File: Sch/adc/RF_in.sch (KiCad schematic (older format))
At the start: 72 parts, among them CN1 SMA, CN2 SMA, J3 JP2, J4 JP2, J5 JP2, J6 JP2, U1 LTC2292, U2 BGA2818, U3 TLV702, U4 BGA2818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

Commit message: Add parts
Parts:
- R13, R14, R15, R2, R3, R5, R6, R7, R8, R9: footprint (none) -> Resistors_SMD:R_0603
- R16: value 51 -> 50; footprint (none) -> Resistors_SMD:R_0603
- R17, R18, R19, R20: value 24.9 -> 25; footprint (none) -> Resistors_SMD:R_0603
- R4: value 50 -> 22; footprint (none) -> Resistors_SMD:R_0603
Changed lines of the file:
@@
 P 6850 1650
 F 0 "R17" V 6930 1650 50  0000 C CNN
-F 1 "24.9" V 6850 1650 50  0000 C CNN
-F 2 "" V 6780 1650 50  0001 C CNN
+F 1 "25" V 6850 1650 50  0000 C CNN
+F 2 "Resistors_SMD:R_0603" V 6780 1650 50  0001 C CNN
 F 3 "" H 6850 1650 50  0000 C CNN
 	1    6850 1650
@@
 P 6850 1950
 F 0 "R18" V 6930 1950 50  0000 C CNN
-F 1 "24.9" V 6850 1950 50  0000 C CNN
-F 2 "" V 6780 1950 50  0001 C CNN
+F 1 "25" V 6850 1950 50  0000 C CNN
+F 2 "Resistors_SMD:R_0603" V 6780 1950 50  0001 C CNN
 F 3 "" H 6850 1950 50  0000 C CNN
 	1    6850 1950
@@
 P 7000 1500
 F 0 "R19" V 7080 1500 50  0000 C CNN
-F 1 "24.9" V 7000 1500 50  0000 C CNN
-F 2 "" V 6930 1500 50  0001 C CNN
+F 1 "25" V 7000 1500 50  0000 C CNN
+F 2 "Resistors_SMD:R_0603" V 6930 1500 50  0001 C CNN
 F 3 "" H 7000 1500 50  0000 C CNN
 	1    7000 1500
@@
 P 7000 2100
 F 0 "R20" V 7080 2100 50  0000 C CNN
-F 1 "24.9" V 7000 2100 50  0000 C CNN
-F 2 "" V 6930 2100 50  0001 C CNN
+F 1 "25" V 7000 2100 50  0000 C CNN
+F 2 "Resistors_SMD:R_0603" V 6930 2100 50  0001 C CNN
 F 3 "" H 7000 2100 50  0000 C CNN
 	1    7000 2100
@@
 P 6450 2200
 F 0 "R16" V 6530 2200 50  0000 C CNN
-F 1 "51" V 6450 2200 50  0000 C CNN
-F 2 "" V 6380 2200 50  0001 C CNN
+F 1 "50" V 6450 2200 50  0000 C CNN
+F 2 "Resistors_SMD:R_0603" V 6380 2200 50  0001 C CNN
 F 3 "" H 6450 2200 50  0000 C CNN
 	1    6450 2200
@@
 F 0 "R15" V 3880 1950 50  0000 C CNN
 F 1 "DNL" V 3800 1950 50  0000 C CNN
-F 2 "" V 3730 1950 50  0001 C CNN
+F 2 "Resistors_SMD:R_0603" V 3730 1950 50  0001 C CNN
 F 3 "" H 3800 1950 50  0000 C CNN
 	1    3800 1950
@@
 F 0 "R2" V 1530 6100 50  0000 C CNN
 F 1 "10k" V 1450 6100 50  0000 C CNN
-F 2 "" V 1380 6100 50  0001 C CNN
+F 2 "Resistors_SMD:R_0603" V 1380 6100 50  0001 C CNN
 F 3 "" H 1450 6100 50  0000 C CNN
 	1    1450 6100
@@
 P 2300 4750
 F 0 "R4" V 2380 4750 50  0000 C CNN
-F 1 "50" V 2300 4750 50  0000 C CNN
-F 2 "" V 2230 4750 50  0001 C CNN
+F 1 "22" V 2300 4750 50  0000 C CNN
+F 2 "Resistors_SMD:R_0603" V 2230 4750 50  0001 C CNN
 F 3 "" H 2300 4750 50  0000 C CNN
 	1    2300 4750
@@
 F 0 "R3" H 1230 4600 50  0000 C CNN
 F 1 "10k" V 1150 4600 50  0000 C CNN
-F 2 "" V 1080 4600 50  0001 C CNN
+F 2 "Resistors_SMD:R_0603" V 1080 4600 50  0001 C CNN
 F 3 "" H 1150 4600 50  0000 C CNN
 	1    1150 4600
@@
 F 0 "R8" V 7380 3500 50  0000 C CNN
 F 1 "25" V 7300 3500 50  0000 C CNN
-F 2 "" V 7230 3500 50  0001 C CNN
+F 2 "Resistors_SMD:R_0603" V 7230 3500 50  0001 C CNN
 F 3 "" H 7300 3500 50  0000 C CNN
 	1    7300 3500
@@
 F 0 "R7" V 7380 3200 50  0000 C CNN
 F 1 "25" V 7300 3200 50  0000 C CNN
-F 2 "" V 7230 3200 50  0001 C CNN
+F 2 "Resistors_SMD:R_0603" V 7230 3200 50  0001 C CNN
 F 3 "" H 7300 3200 50  0000 C CNN
 	1    7300 3200
@@
 F 0 "R5" V 6830 2900 50  0000 C CNN
 F 1 "1k" V 6750 2900 50  0000 C CNN
-F 2 "" V 6680 2900 50  0001 C CNN
+F 2 "Resistors_SMD:R_0603" V 6680 2900 50  0001 C CNN
 F 3 "" H 6750 2900 50  0000 C CNN
 	1    6750 2900
@@
 F 0 "R6" V 7080 2900 50  0000 C CNN
 F 1 "1k" V 7000 2900 50  0000 C CNN
-F 2 "" V 6930 2900 50  0001 C CNN
+F 2 "Resistors_SMD:R_0603" V 6930 2900 50  0001 C CNN
 F 3 "" H 7000 2900 50  0000 C CNN
 	1    7000 2900
@@
 F 0 "R9" V 2530 4250 50  0000 C CNN
 F 1 "10k" V 2450 4250 50  0000 C CNN
-F 2 "" V 2380 4250 50  0001 C CNN
+F 2 "Resistors_SMD:R_0603" V 2380 4250 50  0001 C CNN
 F 3 "" H 2450 4250 50  0000 C CNN
 	1    2450 4250
@@
 F 0 "R13" V 4530 4650 50  0000 C CNN
 F 1 "22" V 4450 4650 50  0000 C CNN
-F 2 "" V 4380 4650 50  0001 C CNN
+F 2 "Resistors_SMD:R_0603" V 4380 4650 50  0001 C CNN
 F 3 "" H 4450 4650 50  0000 C CNN
 	1    4450 4650
@@
 F 0 "R14" V 4530 4750 50  0000 C CNN
 F 1 "22" V 4450 4750 50  0000 C CNN
-F 2 "" V 4380 4750 50  0001 C CNN
+F 2 "Resistors_SMD:R_0603" V 4380 4750 50  0001 C CNN
 F 3 "" H 4450 4750 50  0000 C CNN
 	1    4450 4750

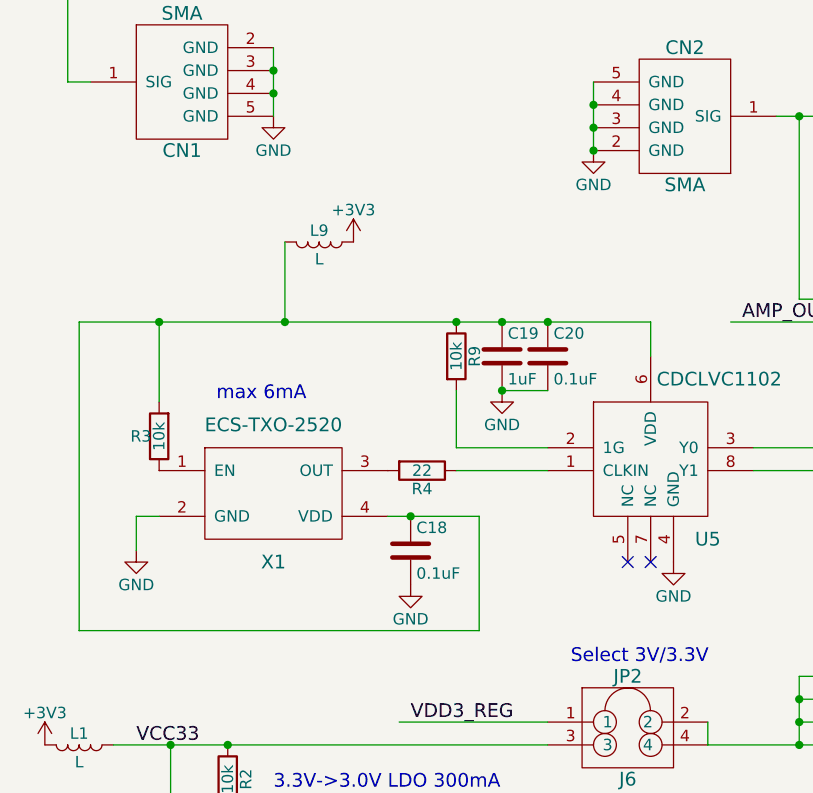
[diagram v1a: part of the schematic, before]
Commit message: Changed TCXO->MEMS TCXO. BOM finished
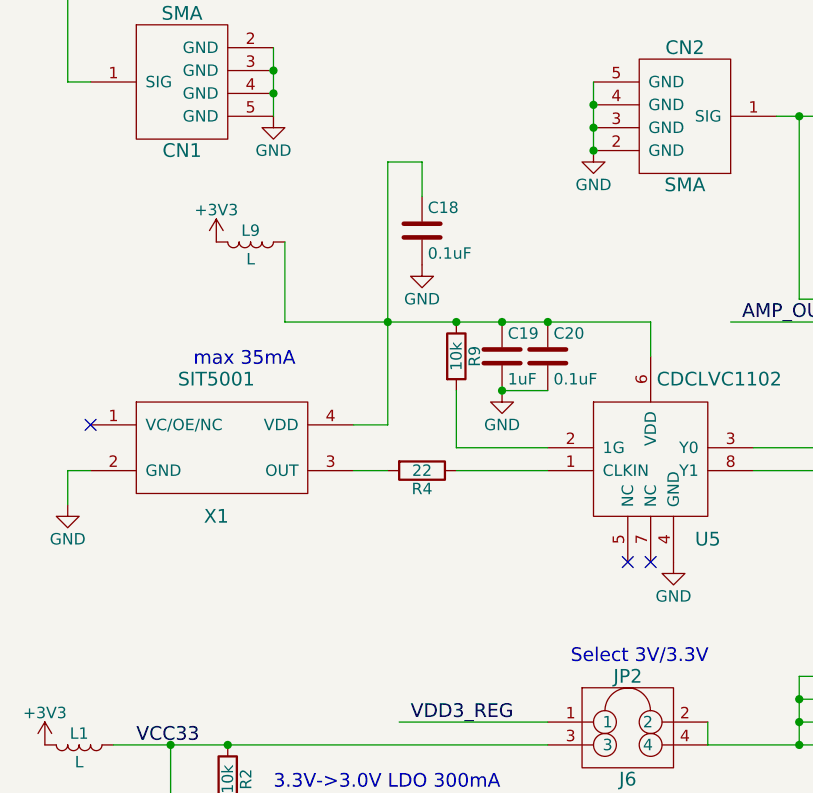
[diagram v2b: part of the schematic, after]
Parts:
- removed R3: 10k, Resistors_SMD:R_0603, symbol R
- removed X1: ECS-TXO-2520, symbol ECS-TXO-2520
- added X1: SIT5001, symbol SIT5001
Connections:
- no-connect marks 6 -> 7
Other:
- note added: "max 35mA"
- note removed: "max 6mA"
- moved on the sheet: C18, L9
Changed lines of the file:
@@
-$EndComp
-$Comp
-L ECS-TXO-2520 X1
-U 1 1 58A5DB2D
-P 1700 4850
-F 0 "X1" H 1650 4550 60  0000 C CNN
-F 1 "ECS-TXO-2520" H 1650 5150 60  0000 C CNN
-F 2 "" H 1700 4700 60  0001 C CNN
-F 3 "" H 1700 4700 60  0001 C CNN
-	1    1700 4850
-	1    0    0    -1
 $EndComp
 $Comp
@@
 L GND #PWR030
 U 1 1 58A651BF
-P 1050 5100
-F 0 "#PWR030" H 1050 4850 50  0001 C CNN
-F 1 "GND" H 1050 4950 50  0000 C CNN
-F 2 "" H 1050 5100 50  0000 C CNN
-F 3 "" H 1050 5100 50  0000 C CNN
-	1    1050 5100
+P 750 4900
+F 0 "#PWR030" H 750 4650 50  0001 C CNN
+F 1 "GND" H 750 4750 50  0000 C CNN
+F 2 "" H 750 4900 50  0000 C CNN
+F 3 "" H 750 4900 50  0000 C CNN
+	1    750  4900
 	1    0    0    -1
 $EndComp
@@
 	0    1    1    0
 $EndComp
-$Comp
-L R R3
-U 1 1 58A67F71
-P 1150 4600
-F 0 "R3" H 1230 4600 50  0000 C CNN
-F 1 "10k" V 1150 4600 50  0000 C CNN
-F 2 "Resistors_SMD:R_0603" V 1080 4600 50  0001 C CNN
-F 3 "" H 1150 4600 50  0000 C CNN
-	1    1150 4600
-	-1   0    0    1
-$EndComp
 Text Label 7250 2550 0    60   ~ 0
 CLK40M
@@
 Connection ~ 3950 5950
 Wire Wire Line
-	1150 4950 1050 4950
-Wire Wire Line
-	1050 4950 1050 5100
+	850  4750 750  4750
+Wire Wire Line
+	750  4750 750  4900
 Connection ~ 1200 5950
 Wire Wire Line
 	1450 6250 1450 6650
-Wire Wire Line
-	2150 4950 2550 4950
 Wire Wire Line
 	2450 4750 2850 4750
@@
 $EndComp
 Wire Wire Line
-	800  4100 3300 4100
+	1700 4100 3300 4100
 $Comp
 L +3V3 #PWR046
 U 1 1 58A88C4E
-P 2000 3750
-F 0 "#PWR046" H 2000 3600 50  0001 C CNN
-F 1 "+3V3" H 2000 3890 50  0000 C CNN
-F 2 "" H 2000 3750 50  0000 C CNN
-F 3 "" H 2000 3750 50  0000 C CNN
-	1    2000 3750
+P 1400 3750
+F 0 "#PWR046" H 1400 3600 50  0001 C CNN
+F 1 "+3V3" H 1400 3890 50  0000 C CNN
+F 2 "" H 1400 3750 50  0000 C CNN
+F 3 "" H 1400 3750 50  0000 C CNN
+	1    1400 3750
 	1    0    0    -1
 $EndComp
@@
 L L L9
 U 1 1 58A8A3F4
-P 1850 3750
-F 0 "L9" V 1800 3750 50  0000 C CNN
-F 1 "L" V 1925 3750 50  0000 C CNN
-F 2 "" H 1850 3750 50  0001 C CNN
-F 3 "" H 1850 3750 50  0000 C CNN
-	1    1850 3750
+P 1550 3750
+F 0 "L9" V 1500 3750 50  0000 C CNN
+F 1 "L" V 1625 3750 50  0000 C CNN
+F 2 "" H 1550 3750 50  0001 C CNN
+F 3 "" H 1550 3750 50  0000 C CNN
+	1    1550 3750
 	0    1    1    0
 $EndComp
-Wire Wire Line
-	1150 4450 1150 4100
-Wire Wire Line
-	2550 4950 2550 5450
-Wire Wire Line
-	2550 5450 800  5450
-Wire Wire Line
-	800  5450 800  4100
-Connection ~ 1150 4100
 $Comp
 L GND #PWR048
 U 1 1 58A8B1A7
-P 2250 5250
-F 0 "#PWR048" H 2250 5000 50  0001 C CNN
-F 1 "GND" H 2250 5100 50  0000 C CNN
-F 2 "" H 2250 5250 50  0000 C CNN
-F 3 "" H 2250 5250 50  0000 C CNN
-	1    2250 5250
+P 2300 3850
+F 0 "#PWR048" H 2300 3600 50  0001 C CNN
+F 1 "GND" H 2300 3700 50  0000 C CNN
+F 2 "" H 2300 3850 50  0000 C CNN
+F 3 "" H 2300 3850 50  0000 C CNN
+	1    2300 3850
 	1    0    0    -1
 $EndComp
@@
 L C C18
 U 1 1 58A8B24F
-P 2250 5100
-F 0 "C18" H 2275 5200 50  0000 L CNN
-F 1 "0.1uF" H 2275 5000 50  0000 L CNN
-F 2 "Capacitors_SMD:C_0402" H 2288 4950 50  0001 C CNN
-F 3 "" H 2250 5100 50  0000 C CNN
-	1    2250 5100
-	1    0    0    -1
-$EndComp
-Connection ~ 2250 4950
+P 2300 3700
+F 0 "C18" H 2325 3800 50  0000 L CNN
+F 1 "0.1uF" H 2325 3600 50  0000 L CNN
+F 2 "Capacitors_SMD:C_0402" H 2338 3550 50  0001 C CNN
+F 3 "" H 2300 3700 50  0000 C CNN
+	1    2300 3700
+	1    0    0    -1
+$EndComp
 NoConn ~ 3200 5150
 NoConn ~ 3300 5150
@@
 Text Notes 7500 700  0    60   ~ 0
 VDD: 2Vp-p,\nVCM: 1Vp-p
-Text Notes 1400 4450 0    60   ~ 0
-max 6mA
+Text Notes 1300 4300 0    60   ~ 0
+max 35mA
 $Comp
 L GND #PWR050
@@
 Wire Wire Line
 	1700 4100 1700 3750
-Connection ~ 1700 4100
 Text Label 1050 5950 0    60   ~ 0
 VCC33
@@
 Text Label 4550 5350 0    60   ~ 0
 VCC33
+$Comp
+L SIT5001 X1
+U 1 1 58AAF16C
+P 1400 4650
+F 0 "X1" H 1400 4350 60  0000 C CNN
+F 1 "SIT5001" H 1400 4950 60  0000 C CNN
+F 2 "" H 1200 4650 60  0001 C CNN
+F 3 "" H 1200 4650 60  0001 C CNN
+	1    1400 4650
+	1    0    0    -1
+$EndComp
+NoConn ~ 850  4550
+Wire Wire Line
+	2300 3550 2300 3400
+Wire Wire Line
+	2300 3400 2150 3400
+Wire Wire Line
+	2150 3400 2150 4550
+Connection ~ 2150 4100
+Wire Wire Line
+	2150 4550 2000 4550
+Wire Wire Line
+	2150 4750 2000 4750
 $EndSCHEMATC

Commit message: Assigned footprint to all the parts
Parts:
- C1, C12, C15, C16, C17, C19, C2, C20, C22, C23, C24, C25, C26, C37, C38, C39, C9: footprint Capacitors_SMD:C_0603 -> adc_lib:C0603
- C10, C11, C13, C14, C18, C29, C30, C31, C32, C33, C34, C35, C36, C4, C40, C5, C6, C7, C8: footprint Capacitors_SMD:C_0402 -> adc_lib:C0402
- CN1, CN2: footprint (none) -> adc_lib:SMA_RightAngle
- J3, J4, J5, J6: footprint Pin_Headers:Pin_Header_Straight_2x02_Pitch2.54mm -> adc_lib:M20-9980245
- L1, L5, L6, L9: footprint (none) -> adc_lib:FB0805
- L2, L3, L4: footprint (none) -> adc_lib:L0603
- R13, R14, R15, R16, R17, R18, R19, R2, R20, R4, R5, R6, R7, R8, R9: footprint Resistors_SMD:R_0603 -> adc_lib:R0603
- RFTransformer1: footprint (none) -> adc_lib:MABAES0060
- U1: footprint (none) -> adc_lib:LTC2292
- U2, U4: footprint (none) -> adc_lib:BGA2818
- U3: footprint (none) -> adc_lib:TLV702
- U5: footprint (none) -> adc_lib:CDCLVC1102
- X1: footprint (none) -> adc_lib:SIT5001

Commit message: Routing in progress
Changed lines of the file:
@@
 Text Label 8550 5400 0    60   ~ 0
 VCMB
-Text GLabel 5000 4750 2    60   Output ~ 0
+Text GLabel 5000 4650 2    60   Output ~ 0
 ADC_CLK
 $Comp
@@
 Wire Wire Line
 	3750 4650 4300 4650
-Text Label 4650 4650 0    60   ~ 0
+Text Label 4650 4750 0    60   ~ 0
 CLK40M
 Wire Wire Line

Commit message: done except GND net
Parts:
- added L11: L, adc_lib:FB0805, symbol L
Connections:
- net labels removed: VCC
- wire segments 142 -> 143
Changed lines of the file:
@@
 Wire Wire Line
 	5350 2750 4750 2750
-Text Label 2250 750  0    60   ~ 0
-VCC
-Text Label 4850 2750 0    60   ~ 0
-VCC
 $Comp
 L C C9
@@
 Wire Wire Line
 	2150 4750 2000 4750
+$Comp
+L +3V3 #PWR052
+U 1 1 58B47FF2
+P 4300 2750
+F 0 "#PWR052" H 4300 2600 50  0001 C CNN
+F 1 "+3V3" H 4300 2890 50  0000 C CNN
+F 2 "" H 4300 2750 50  0000 C CNN
+F 3 "" H 4300 2750 50  0000 C CNN
+	1    4300 2750
+	1    0    0    -1
+$EndComp
+$Comp
+L L L11
+U 1 1 58B47FF8
+P 4600 2750
+F 0 "L11" V 4550 2750 50  0000 C CNN
+F 1 "L" V 4675 2750 50  0000 C CNN
+F 2 "adc_lib:FB0805" H 4600 2750 50  0001 C CNN
+F 3 "" H 4600 2750 50  0000 C CNN
+	1    4600 2750
+	0    1    1    0
+$EndComp
+Wire Wire Line
+	4450 2750 4300 2750
 $EndSCHEMATC

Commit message: Apply some design rules
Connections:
- wire segments 143 -> 144
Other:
- moved on the sheet: C25
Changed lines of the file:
@@
 L GND #PWR018
 U 1 1 58A1C6CA
-P 2450 1050
-F 0 "#PWR018" H 2450 800 50  0001 C CNN
-F 1 "GND" H 2450 900 50  0000 C CNN
-F 2 "" H 2450 1050 50  0000 C CNN
-F 3 "" H 2450 1050 50  0000 C CNN
-	1    2450 1050
+P 2350 1150
+F 0 "#PWR018" H 2350 900 50  0001 C CNN
+F 1 "GND" H 2350 1000 50  0000 C CNN
+F 2 "" H 2350 1150 50  0000 C CNN
+F 3 "" H 2350 1150 50  0000 C CNN
+	1    2350 1150
 	1    0    0    -1
 $EndComp
@@
 L C C25
 U 1 1 58A1C6F8
-P 2450 900
-F 0 "C25" H 2475 1000 50  0000 L CNN
-F 1 "22nF" H 2475 800 50  0000 L CNN
-F 2 "adc_lib:C0603" H 2488 750 50  0001 C CNN
-F 3 "" H 2450 900 50  0000 C CNN
-	1    2450 900
+P 2350 1000
+F 0 "C25" H 2375 1100 50  0000 L CNN
+F 1 "22nF" H 2375 900 50  0000 L CNN
+F 2 "adc_lib:C0603" H 2388 850 50  0001 C CNN
+F 3 "" H 2350 1000 50  0000 C CNN
+	1    2350 1000
 	-1   0    0    1
 $EndComp
@@
 Wire Wire Line
 	2950 750  2950 1150
-Connection ~ 2450 750
 Wire Wire Line
 	1600 1600 1850 1600
@@
 Wire Wire Line
 	4450 2750 4300 2750
+Wire Wire Line
+	2350 850  2350 750
+Connection ~ 2350 750
 $EndSCHEMATC
